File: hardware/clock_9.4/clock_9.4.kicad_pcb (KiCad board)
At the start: 2 copper layers, 119 x 92 mm, 64 parts, among them J2 Conn_01x03, J4 USB_C_Receptacle, J5 Conn_01x06_Pin, J8 Conn_01x02, Q2 S8550, Q3 S8050, U10 STM32F405RGTx, U11 AMS1117-3.3, U12 BA50DD0WHFP-TR, U14 CH340C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

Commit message: clean up simple 9.4 for new power supply
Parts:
- removed C27: 100n, Capacitor_SMD:C_0603_1608Metric
- removed J5: Conn_01x06_Pin, Connector_PinHeader_2.54mm:PinHeader_1x06_P2.54mm_Vertical
- removed Q2: S8550, Package_TO_SOT_SMD:SOT-23
- removed Q3: S8050, Package_TO_SOT_SMD:SOT-23
- removed R27, R28: 4K7, Resistor_SMD:R_0603_1608Metric
- removed R41, R42, R54, R56, R57, R62, R65, R66, R67, R68: 1K0, Resistor_SMD:R_0603_1608Metric
- removed R58, R59: 1K5, Resistor_SMD:R_0603_1608Metric
- removed S3: 147873-2, blinky_footprints:SW_147873-2
- added C1: 100n, Capacitor_SMD:C_0402_1005Metric, F.Cu at (154.7, 44.1)
- added C2: 100n, Capacitor_SMD:C_0402_1005Metric, F.Cu at (160.9, 52.3)
- added C3: 100n, Capacitor_SMD:C_0402_1005Metric, F.Cu at (155.8, 51.2)
- added C4: 100n, Capacitor_SMD:C_0603_1608Metric, F.Cu at (175.6, 44.5)
- added JP3: SolderJumper_2_Bridged, Jumper:SolderJumper-2_P1.3mm_Bridged2Bar_RoundedPad1.0x1.5mm, F.Cu at (157.4, 105.6)
- added R1: 330R, Resistor_SMD:R_0603_1608Metric, F.Cu at (158.0, 47.7)
- added R2: 330R, Resistor_SMD:R_0603_1608Metric, F.Cu at (164.8, 51.7)
- added R3: 4K7, Resistor_SMD:R_0603_1608Metric, F.Cu at (193.2, 45.1)
- added R4: 4K7, Resistor_SMD:R_0603_1608Metric, F.Cu at (175.6, 46.5)
- added S2: 147873-2, blinky_footprints:SW_147873-2, F.Cu at (168.5, 45.5)
- added TP1: ~, TestPoint:TestPoint_THTPad_D1.5mm_Drill0.7mm, F.Cu at (150.4, 54.1)
- added TP10: ~, TestPoint:TestPoint_THTPad_D1.5mm_Drill0.7mm, F.Cu at (119.4, 128.0)
- added TP11: ~, TestPoint:TestPoint_THTPad_D1.5mm_Drill0.7mm, F.Cu at (146.9, 127.9)
- added TP2: ~, TestPoint:TestPoint_THTPad_D1.5mm_Drill0.7mm, F.Cu at (149.7, 46.7)
- added TP3: ~, TestPoint:TestPoint_THTPad_D1.5mm_Drill0.7mm, F.Cu at (192.3, 41.0)
- added TP4: ~, TestPoint:TestPoint_THTPad_D1.5mm_Drill0.7mm, F.Cu at (173.8, 41.1)
- added TP5: ~, TestPoint:TestPoint_THTPad_D1.5mm_Drill0.7mm, F.Cu at (124.0, 128.0)
- added TP6: ~, TestPoint:TestPoint_THTPad_D1.5mm_Drill0.7mm, F.Cu at (137.3, 127.9)
- added TP7: ~, TestPoint:TestPoint_THTPad_D1.5mm_Drill0.7mm, F.Cu at (141.8, 128.0)
- added TP8: ~, TestPoint:TestPoint_THTPad_D1.5mm_Drill0.7mm, F.Cu at (128.2, 128.0)
- added TP9: ~, TestPoint:TestPoint_THTPad_D1.5mm_Drill0.7mm, F.Cu at (133.1, 127.9)
- added U1: SN74LVC1G14DBV, Package_TO_SOT_SMD:SOT-23-5, F.Cu at (155.1, 54.0)
- added U2: SN74LVC1G14DBV, Package_TO_SOT_SMD:SOT-23-5, F.Cu at (154.1, 46.7)
- added U3: SN74LVC1G14DBV, Package_TO_SOT_SMD:SOT-23-5, F.Cu at (160.3, 54.9)
- moved JP2 18.3 mm to (168.1, 49.0), turned to 0 degrees
- moved S1 17.6 mm to (186.2, 45.0)
- moved JP1 14.6 mm to (161.9, 47.7)
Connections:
- C44 pad 1: +6V -> Net-(JP3-B)
- JP1 pad 1: /NRST -> Net-(JP1-A)
- JP1 pad 2: Net-(JP1-B) -> /BOOT0
- JP2 pad 1: /BOOT0 -> Net-(JP2-A)
- JP2 pad 2: Net-(JP2-B) -> /NRST
- JP5 pad 2: +6V -> Net-(JP3-B)
- S1 pad 1: /NRST -> /BOOT0
- S1 pad 2: GND -> +3.3V
- U10 pad 14: Net-(U10-PA0) -> unconnected-(U10-PA0-Pad14)
- U10 pad 50: Net-(U10-PA15) -> unconnected-(U10-PA15-Pad50)
- U12 pad 2: +6V -> Net-(JP3-B)
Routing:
- net Net-(U10-PA15): track 82.7 -> 0.00 mm, vias 2 -> 0
- net Net-(JP3-B): track 0.00 -> 58.1 mm, vias 0 -> 2
- net +3.3V: track 335.5 -> 392.4 mm, vias 15 -> 17
- net +5V: track 2.72 -> 59.0 mm, vias 0 -> 2
- net /LED10: track 56.2 -> 0.00 mm, vias 4 -> 0
- net GND: track 684.1 -> 739.9 mm, vias 28 -> 32
- net +5VA: track 4.05 -> 58.1 mm, vias 0 -> 2
- net Net-(U10-PA0): track 50.1 -> 0.00 mm, vias 4 -> 0
- net /LED9: track 49.1 -> 0.00 mm, vias 4 -> 0
- net Net-(Q2-B): track 29.0 -> 0.00 mm, vias 2 -> 0
- net /PPS_OUT: track 27.4 -> 0.00 mm, vias 2 -> 0
- net Net-(Q3-B): track 22.9 -> 0.00 mm, vias 2 -> 0
- net /AUX_MON_PPS: track 20.8 -> 0.00 mm, vias 2 -> 0
- net /USB_RTS: track 71.8 -> 92.3 mm
- net /DB3: track 16.8 -> 0.00 mm
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
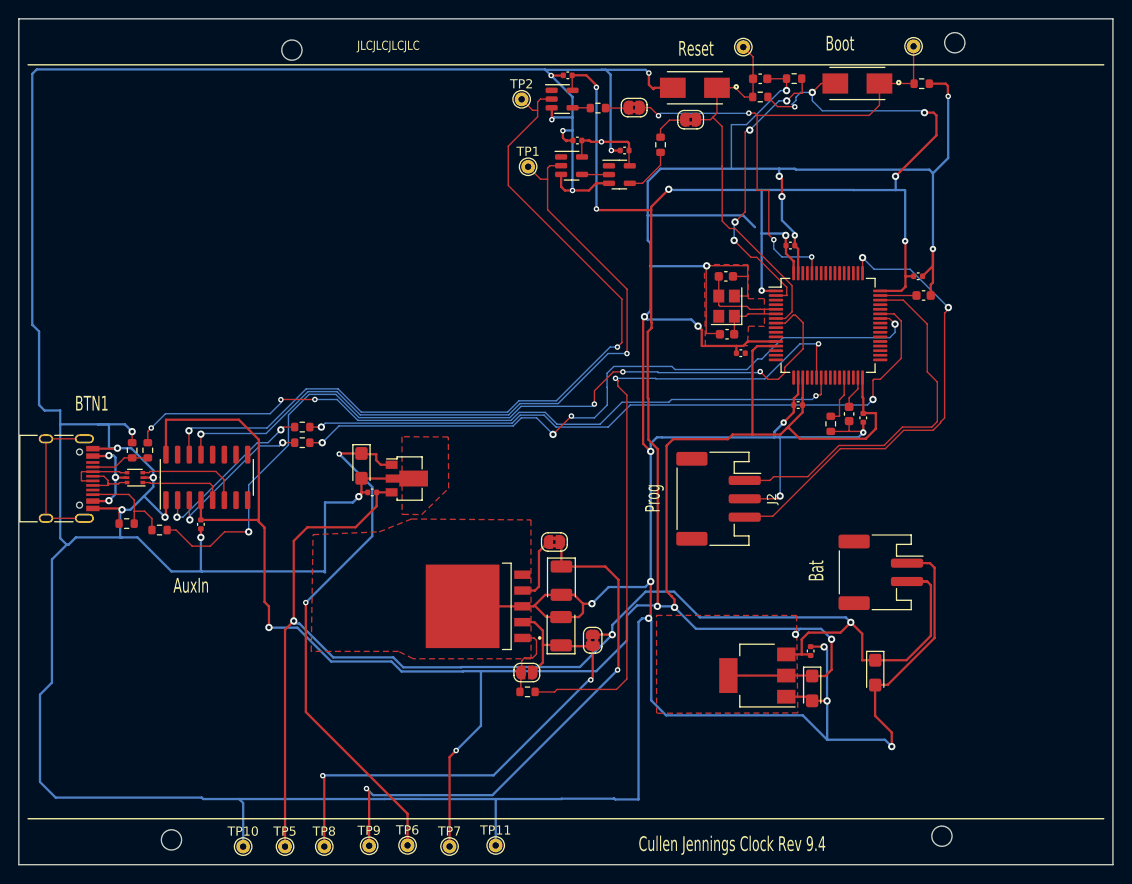
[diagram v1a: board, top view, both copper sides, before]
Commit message: do v9.4 board with new power reg
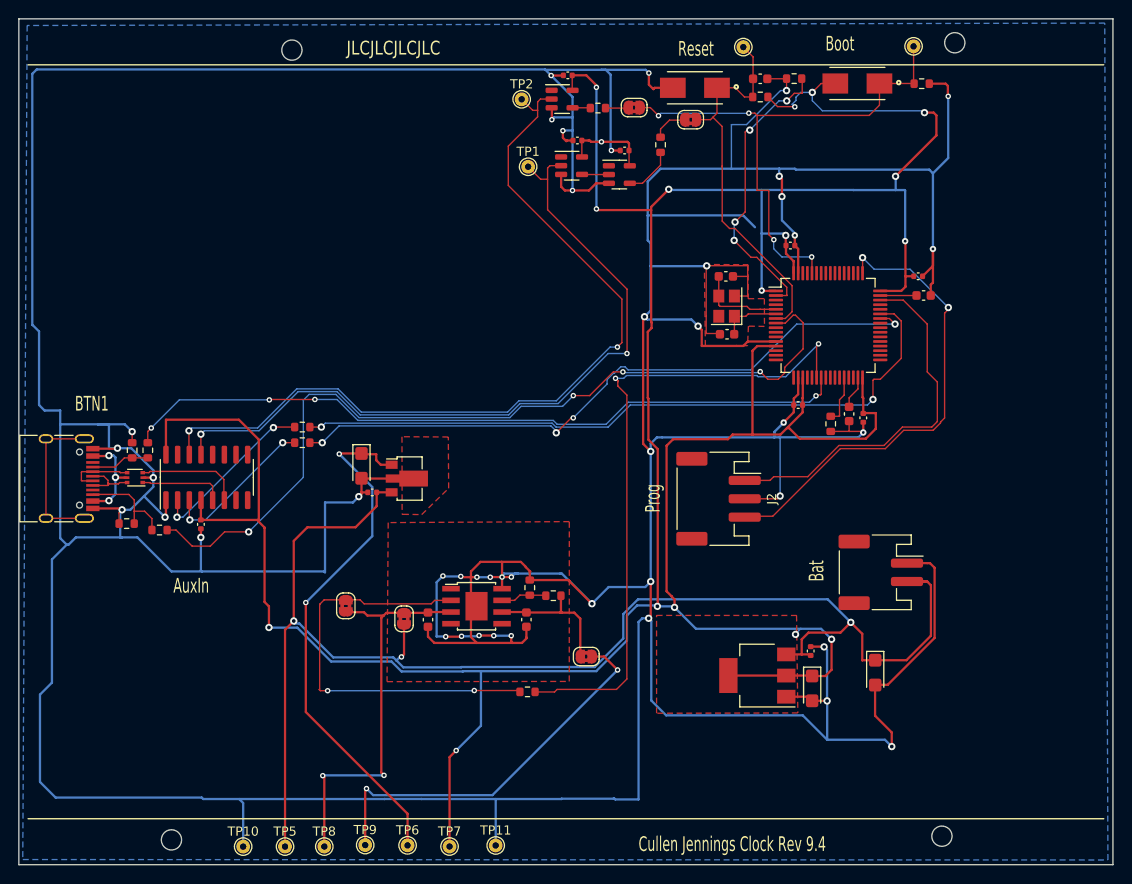
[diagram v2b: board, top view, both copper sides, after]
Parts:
- removed C30: 100n, Capacitor_SMD:C_0402_1005Metric
- removed C42, C44: 33u, Capacitor_Tantalum_SMD:CP_EIA-3528-21_Kemet-B
- removed U12: BA50DD0WHFP-TR, blinky_footprints:DPAK172P1054X200-6N
- added C5: 10u, Capacitor_SMD:C_0603_1608Metric, F.Cu at (139.5, 103.3)
- added C6: 10u, Capacitor_SMD:C_0603_1608Metric, F.Cu at (150.2, 103.3)
- added R5: 274K, Resistor_SMD:R_0603_1608Metric, F.Cu at (153.1, 100.7)
- added R6: 30K, Resistor_SMD:R_0603_1608Metric, F.Cu at (150.6, 99.9)
- added U4: TPS7A7001DDA, Package_SO:TI_SO-PowerPAD-8, F.Cu at (144.8, 101.9)
- JP5: value SolderJumper_2_Open -> SolderJumper_2_Bridged; footprint Jumper:SolderJumper-2_P1.3mm_Open_RoundedPad1.0x1.5mm -> Jumper:SolderJumper-2_P1.3mm_Bridged2Bar_RoundedPad1.0x1.5mm
- moved JP4 23.7 mm to (130.6, 101.8), turned to -90 degrees
- moved JP3 20.7 mm to (136.9, 103.3), turned to 90 degrees
- moved JP5 6.70 mm to (156.7, 107.4)
- moved TP9 0.44 mm to (132.7, 127.9)
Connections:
- JP4 pad 2: +5V -> Net-(JP3-B)
- JP5 pad 2: Net-(JP3-B) -> +5V
- R69 pad 1: Net-(JP5-A) -> Net-(JP4-A)
- U10 pad 29: /GPS_PPS -> unconnected-(U10-PB10-Pad29)
- U10 pad 30: /MON_PPS -> unconnected-(U10-PB11-Pad30)
- U10 pad 61: /SCL -> unconnected-(U10-PB8-Pad61)
- U10 pad 62: /SDA -> unconnected-(U10-PB9-Pad62)
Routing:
- net GND: track 739.9 -> 792.5 mm, vias 32 -> 43
- net Net-(JP4-A): track 7.26 -> 46.1 mm, vias 0 -> 2
- net +5V: track 59.0 -> 42.8 mm
- net Net-(JP3-B): track 58.1 -> 43.8 mm
- net Net-(JP5-A): track 8.75 -> 14.8 mm
- net Net-(U4-FB): track 0.00 -> 5.02 mm
- net /USB_RX: track 75.4 -> 72.1 mm
- net +6V: track 152.8 -> 155.2 mm
- net /LED2: track 81.1 -> 80.2 mm
- net /AUD_IN: track 94.2 -> 93.4 mm
- net /USB_TX: track 76.4 -> 75.7 mm
- added copper zone on B.Cu, net GND

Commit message: submitted version of 9.4 board
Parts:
- R5: value 274K -> 270K
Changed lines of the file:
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@@
     (tags "SSOP 0.50 exposed pad")
     (property "JLCPCB Part #" "C60719")
+    (property "JLCPCB Rotation Offset" "270")
     (property "Sheetfile" "clock_9.4.kicad_sch")
     (property "Sheetname" "")
@@
     (descr "Resistor SMD 0603 (1608 Metric), square (rectangular) end terminal, IPC_7351 nominal, (Body size source: IPC-SM-782 page 72, https://www.pcb-3d.com/wordpress/wp-content/uploads/ipc-sm-782a_amendment_1_and_2.pdf), generated with kicad-footprint-generator")
     (tags "resistor")
-    (property "JLCPCB Part #" "")
-    (property "LCSC" "")
+    (property "JLCPCB Part #" "C22984")
     (property "Sheetfile" "clock_9.4.kicad_sch")
     (property "Sheetname" "")
@@
     (tags "connector JST PH top entry")
     (property "JLCPCB Part #" "C265101")
+    (property "JLCPCB Rotation Offset" "180")
     (property "Sheetfile" "clock_9.4.kicad_sch")
     (property "Sheetname" "")
@@
     (descr "Resistor SMD 0603 (1608 Metric), square (rectangular) end terminal, IPC_7351 nominal, (Body size source: IPC-SM-782 page 72, https://www.pcb-3d.com/wordpress/wp-content/uploads/ipc-sm-782a_amendment_1_and_2.pdf), generated with kicad-footprint-generator")
     (tags "resistor")
-    (property "JLCPCB Part #" "")
-    (property "LCSC" "")
+    (property "JLCPCB Part #" "C22966")
     (property "Sheetfile" "clock_9.4.kicad_sch")
     (property "Sheetname" "")
@@
         (effects (font (size 1 1) (thickness 0.15)))
     )
-    (fp_text value "274K" (at 0 1.43) (layer "F.Fab")
+    (fp_text value "270K" (at 0 1.43) (layer "F.Fab")
         (effects (font (size 1 1) (thickness 0.15)))
     )
